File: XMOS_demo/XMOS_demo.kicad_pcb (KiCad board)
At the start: 4 copper layers, 100 x 100 mm, 210 parts, among them J1 XSYS2 DEBUG CONNECTOR, J10 Conn_PMOD_02x06, J11 Conn_PMOD_02x06, J2 Screw_Terminal, J3 Conn_01x02_Pin, J4 USB_C_Receptacle_USB2.0_16P, J5 Conn_01x06_Socket, J6 Conn_01x06_Socket, J7 AudioJack3_SwitchT, J8 AudioJack2_SwitchT, J9 AudioJack2_SwitchT, U1 U316-1024-QF60B, U10 OPA340NA, U11 OPA340NA, U12 AT25FF161A, U3 TPD3S014, U4 TLV75733PDBV, U5 TLV75718PDBV, U6 AP61200Z6, U7 MAX97220C, U8 CS4271, U9 OPA340NA, Y1 Crystal_24M, Y2 24.576M

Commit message: xmos pcb work
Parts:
- TP7: footprint TestPoint:TestPoint_Keystone_5005-5009_Compact -> TestPoint:TestPoint_Pad_D2.0mm
- moved TP5 6.31 mm to (140.6, 142.0)
- moved D5 5.11 mm to (141.8, 148.6)
- moved R19 5.11 mm to (141.8, 145.6)
- moved D6 4.97 mm to (146.9, 148.6)
- moved R20 4.97 mm to (146.9, 145.6)
- moved TP6 4.97 mm to (146.9, 142.0)
- moved C31 0.75 mm to (142.5, 135.6)
- moved TP7 0.62 mm to (185.1, 130.9)
- moved C30 0.32 mm to (184.2, 138.1)
- moved TP10 0.20 mm to (161.3, 129.8)
- moved C37 0.12 mm to (157.8, 131.3)
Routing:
- net P0V9: track 40.2 -> 74.8 mm
- net VBUS_FILT: track 15.8 -> 23.5 mm
- net P1V8: track 44.7 -> 38.1 mm, vias 3 -> 9
- net Net-(U4-IN): track 6.36 -> 8.76 mm
- net VBUS: track 20.6 -> 22.6 mm
- net /Codec/SDA: track 56.6 -> 58.3 mm
- net P3V3: track 38.1 -> 39.5 mm, vias 11 -> 16
- net /MCU/XL0_IN0: track 59.1 -> 58.4 mm
- net P5V0: vias 3 -> 15
- added copper zone on B.Cu, net P1V8
- added copper zone on F.Cu, net P1V8
- added copper zone on B.Cu, net P5V0

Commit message: routing
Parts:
- added H5: M3_NPTH, MountingHole:MountingHole_3.2mm_M3, F.Cu at (119.5, 89.7)
- moved C51 33.1 mm to (137.8, 56.6), turned to 180 degrees
- moved C45 25.7 mm to (135.3, 59.5), turned to 180 degrees
- moved C41 20.4 mm to (135.3, 63.5), turned to 180 degrees
- moved C50 20.1 mm to (137.8, 66.0), turned to 180 degrees
- moved C73 16.5 mm to (162.5, 61.4)
- moved R33 15.0 mm to (120.4, 59.3), turned to 0 degrees
- moved R35 13.6 mm to (120.4, 60.8), turned to 0 degrees
- moved C71 11.8 mm to (166.0, 73.3)
- moved C83 11.8 mm to (163.0, 73.3)
- moved C84 11.8 mm to (164.5, 73.3)
- moved R55 11.8 mm to (167.5, 73.3)
- moved R56 11.8 mm to (166.8, 75.5)
- moved R57 11.8 mm to (158.0, 72.2)
- moved U9 11.8 mm to (160.5, 72.8)
- moved R34 11.3 mm to (126.8, 98.8), turned to 90 degrees
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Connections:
- J5 pad 1: P5V0 -> GND
- J5 pad 2: /Audio Out/OUT_A+ -> /Audio Out/OUT_A-
- J5 pad 3: /Audio Out/OUT_A- -> /Audio Out/OUT_A+
- J5 pad 6: GND -> P5V0
- J6 pad 2: /Audio Out/INR+ -> /Audio Out/INR-
- J6 pad 3: /Audio Out/INR- -> /Audio Out/INR+
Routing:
- net /MCU/CODEC_~{RST}: track 11.2 -> 38.5 mm, vias 0 -> 2
- net GND: track 35.8 -> 62.6 mm, vias 55 -> 62
- net /Audio Out/INR+: track 0.00 -> 25.1 mm
- net /Audio Out/INL+: track 0.00 -> 25.1 mm
- net /Audio Out/OUT_B-: track 0.00 -> 22.9 mm
- net /Audio Out/INR-: track 0.00 -> 21.9 mm
- net /Audio Out/INL-: track 0.00 -> 21.8 mm
- net /Audio Out/OUT_B+: track 0.00 -> 19.6 mm
- net /Audio Out/OUT_A+: track 0.00 -> 17.8 mm
- net /Audio Out/OUT_A-: track 0.00 -> 17.3 mm
- net /Audio In/VQ2_3: track 0.00 -> 15.4 mm
- net /Audio In/VQ1: track 0.00 -> 12.4 mm
- net Net-(U8-FILT+): track 0.00 -> 12.1 mm
- net /Audio Out/~{MUTE}: track 0.00 -> 9.73 mm, vias 0 -> 2
- net Net-(U8-XTI): track 0.00 -> 9.45 mm
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- added copper zone on F.Cu, net Net-(U5-IN)

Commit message: sch and pcb changes - output filter
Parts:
- added C48: 470n, Capacitor_SMD:C_1206_3216Metric_Pad1.33x1.80mm_HandSolder, F.Cu at (135.3, 69.0)
- added C50: 470n, Capacitor_SMD:C_1206_3216Metric_Pad1.33x1.80mm_HandSolder, F.Cu at (111.2, 76.5)
- added C54: 470n, Capacitor_SMD:C_1206_3216Metric_Pad1.33x1.80mm_HandSolder, F.Cu at (135.6, 53.7)
- added C56: 470n, Capacitor_SMD:C_1206_3216Metric_Pad1.33x1.80mm_HandSolder, F.Cu at (96.4, 76.2)
- moved R22 13.9 mm to (149.3, 148.6)
- moved R21 1.66 mm to (149.3, 145.6)
- moved C73 0.91 mm to (163.4, 61.5)
- renumbered C46 to C41, C49 to C42, C53 to C43, C57 to C44, C59 to C45, C60 to C46, C41 to C47, C47 to C49, C50 to C51, C45 to C53, C48 to C55, C51 to C57, C54 to C58, C42 to C59, C43 to C60, C44 to C87, C56 to C88, C58 to C89, C55 to C90, R32 to R31, R34 to R32, R41 to R33, R42 to R34, R37 to R36, R33 to R37, R36 to R38, R31 to R39, R39 to R41, R38 to R42, U7 to U2
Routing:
- net Net-(J4-CC2): track 7.20 -> 10.1 mm
- net Net-(J4-CC1): track 8.22 -> 6.67 mm
- net GND: track 62.6 -> 61.6 mm, vias 62 -> 61
- net VBUS: track 22.6 -> 23.2 mm
- net P5V0: vias 19 -> 26

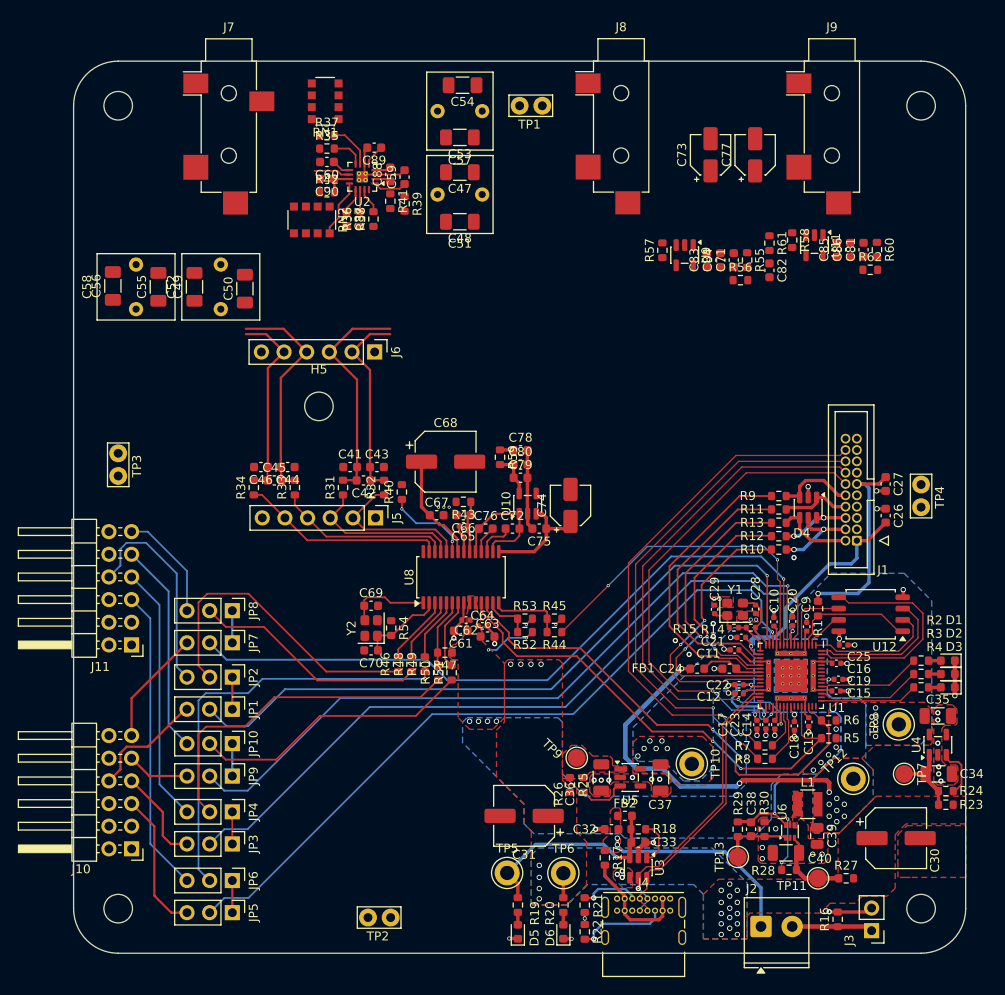
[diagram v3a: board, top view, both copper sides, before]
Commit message: Updated sch and pcb with active filter
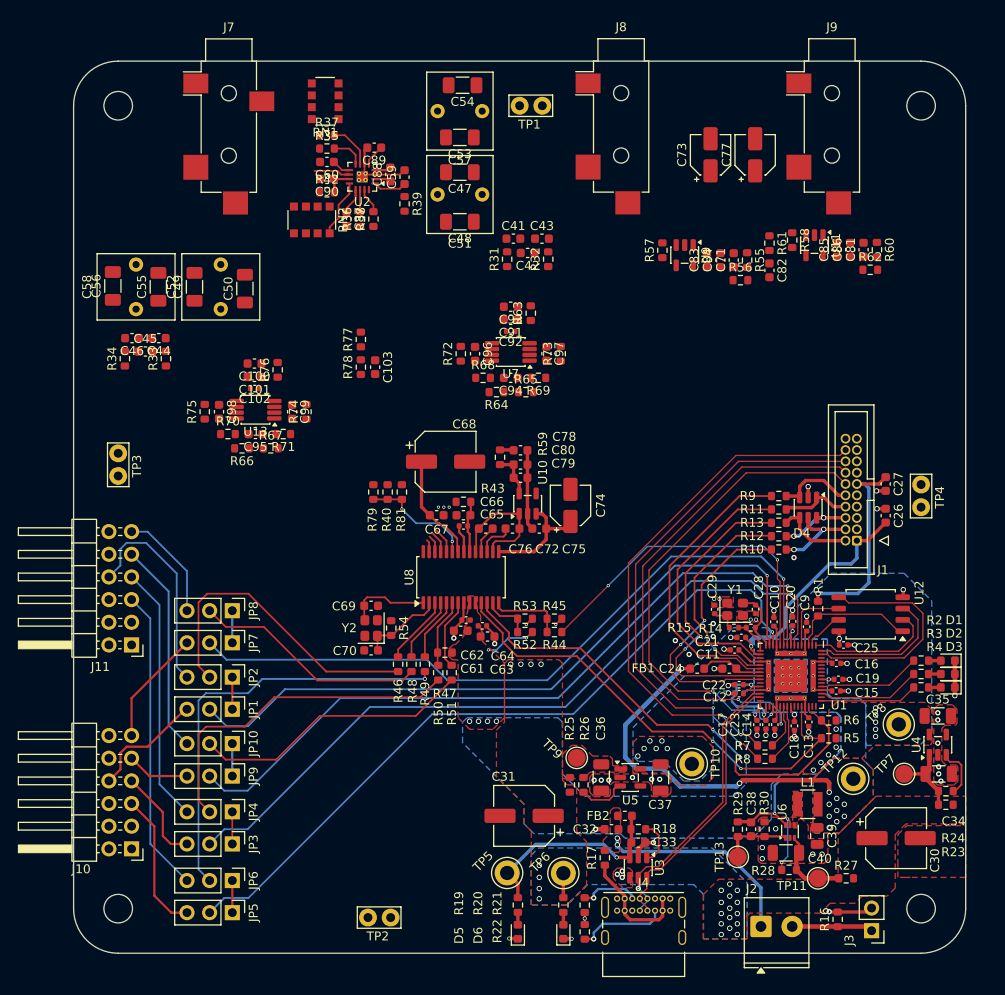
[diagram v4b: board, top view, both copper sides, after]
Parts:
- removed H5: M3_NPTH, MountingHole:MountingHole_3.2mm_M3
- removed J5, J6: Conn_01x06_Socket, Connector_PinHeader_2.54mm:PinHeader_1x06_P2.54mm_Vertical
- removed R41: 10k, Resistor_SMD:R_0603_1608Metric
- added C100: 1u, Capacitor_SMD:C_0603_1608Metric, F.Cu at (112.3, 84.9)
- added C101: 1u, Capacitor_SMD:C_0603_1608Metric, F.Cu at (112.3, 86.4)
- added C102: 100n, Capacitor_SMD:C_0402_1005Metric, F.Cu at (112.3, 87.7)
- added C103: 1u, Capacitor_SMD:C_0603_1608Metric, F.Cu at (125.8, 85.3)
- added C91: 1u, Capacitor_SMD:C_0603_1608Metric, F.Cu at (141.0, 80.0)
- added C92: 100n, Capacitor_SMD:C_0402_1005Metric, F.Cu at (141.0, 81.3)
- added C93: 1u, Capacitor_SMD:C_0603_1608Metric, F.Cu at (141.0, 78.5)
- added C94: 680p, Capacitor_SMD:C_0603_1608Metric, F.Cu at (141.0, 86.5)
- added C95: 680p, Capacitor_SMD:C_0603_1608Metric, F.Cu at (112.4, 92.8)
- added C96: 220p, Capacitor_SMD:C_0603_1608Metric, F.Cu at (137.0, 83.8)
- added C97: 220p, Capacitor_SMD:C_0603_1608Metric, F.Cu at (145.0, 83.8)
- added C98: 220p, Capacitor_SMD:C_0603_1608Metric, F.Cu at (108.3, 90.3)
- added C99: 220p, Capacitor_SMD:C_0603_1608Metric, F.Cu at (116.5, 90.3)
- added R63: 0R, Resistor_SMD:R_0603_1608Metric, F.Cu at (143.2, 79.3)
- added R64: 4k3, Resistor_SMD:R_0603_1608Metric, F.Cu at (139.4, 88.1)
- added R65: 4k3, Resistor_SMD:R_0603_1608Metric, F.Cu at (142.7, 88.1)
- added R66: 4k3, Resistor_SMD:R_0603_1608Metric, F.Cu at (110.9, 94.4)
- added R67: 4k3, Resistor_SMD:R_0603_1608Metric, F.Cu at (114.1, 94.4)
- added R68: 9k1, Resistor_SMD:R_0603_1608Metric, F.Cu at (137.9, 86.5)
- added R69: 9k1, Resistor_SMD:R_0603_1608Metric, F.Cu at (144.1, 86.5)
- added R70: 9k1, Resistor_SMD:R_0603_1608Metric, F.Cu at (109.3, 92.8)
- added R71: 9k1, Resistor_SMD:R_0603_1608Metric, F.Cu at (115.5, 92.8)
- added R72: 4k3, Resistor_SMD:R_0603_1608Metric, F.Cu at (135.4, 83.8)
- added R73: 4k3, Resistor_SMD:R_0603_1608Metric, F.Cu at (146.6, 83.8)
- added R74: 4k3, Resistor_SMD:R_0603_1608Metric, F.Cu at (118.1, 90.3)
- added R75: 4k3, Resistor_SMD:R_0603_1608Metric, F.Cu at (106.7, 90.3)
- added R76: 0R, Resistor_SMD:R_0603_1608Metric, F.Cu at (114.9, 85.6)
- added R77: 10k, Resistor_SMD:R_0603_1608Metric, F.Cu at (124.2, 82.2)
- added R78: 10k, Resistor_SMD:R_0603_1608Metric, F.Cu at (124.2, 85.3)
- added R79: 0R, Resistor_SMD:R_0603_1608Metric, F.Cu at (125.6, 99.3)
- added R81: 10k, Resistor_SMD:R_0603_1608Metric, F.Cu at (128.8, 99.3)
- added U13: OPA1637, Package_SO:VSSOP-8_3x3mm_P0.65mm, F.Cu at (112.4, 90.1)
- added U7: OPA1637, Package_SO:VSSOP-8_3x3mm_P0.65mm, F.Cu at (141.0, 83.6)
- R31, R32, R33, R34: value 634R -> 0R
- moved C43 31.6 mm to (144.5, 70.9)
- moved R31 31.5 mm to (140.6, 73.2)
- moved R32 31.5 mm to (145.2, 73.2)
- moved C41 31.5 mm to (141.3, 70.9)
- moved C42 31.4 mm to (142.9, 72.5)
- moved C44 20.4 mm to (101.5, 82.0)
- moved C45 20.4 mm to (100.0, 83.5)
- moved C46 20.4 mm to (98.5, 82.0)
- moved R33 20.4 mm to (102.3, 84.3)
- moved R34 20.4 mm to (97.8, 84.3)
- moved R40 1.60 mm to (127.2, 99.3)
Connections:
- net Net-(U2-~{SHDN}) renamed /Audio Out/AMP_~{SHDN}
- R31 pad 1: /Audio Out/OUT_A+ -> /Audio Out/OUT_A_FLT+
- R32 pad 1: /Audio Out/OUT_A- -> /Audio Out/OUT_A_FLT-
- R33 pad 1: /Audio Out/OUT_B+ -> /Audio Out/OUT_B_FLT+
- R34 pad 1: /Audio Out/OUT_B- -> /Audio Out/OUT_B_FLT-
- U8 pad 24: /Audio Out/OUT_A- -> /Codec/OUT_A-
- U8 pad 25: /Audio Out/OUT_A+ -> /Codec/OUT_A+
- U8 pad 26: /Audio Out/OUT_B+ -> /Codec/OUT_B+
- U8 pad 27: /Audio Out/OUT_B- -> /Codec/OUT_B-
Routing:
- net /Audio Out/INR+: track 25.1 -> 0.04 mm
- net /Audio Out/INL+: track 25.1 -> 0.07 mm
- net /Audio Out/OUT_B-: track 22.9 -> 0.00 mm
- net /Audio Out/INR-: track 21.9 -> 0.07 mm
- net /Audio Out/INL-: track 21.8 -> 0.07 mm
- net /Audio Out/OUT_B+: track 19.6 -> 0.00 mm
- net /Audio Out/OUT_A+: track 17.8 -> 0.00 mm
- net /Audio Out/OUT_A-: track 17.3 -> 0.00 mm
- net /Audio Out/~{MUTE}: track 9.73 -> 13.0 mm
- net /Codec/OUT_A-: track 0.00 -> 3.01 mm
- net /Codec/OUT_A+: track 0.00 -> 2.48 mm
- net /Codec/OUT_B+: track 0.00 -> 1.94 mm
- net /Codec/OUT_B-: track 0.00 -> 1.39 mm
